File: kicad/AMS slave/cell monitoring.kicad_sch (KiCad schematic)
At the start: 78 parts, among them J1 Conn_02x08_Top_Bottom, Q1 KY2N7002, SW1 SW_Push, U1 BQ76940DBT

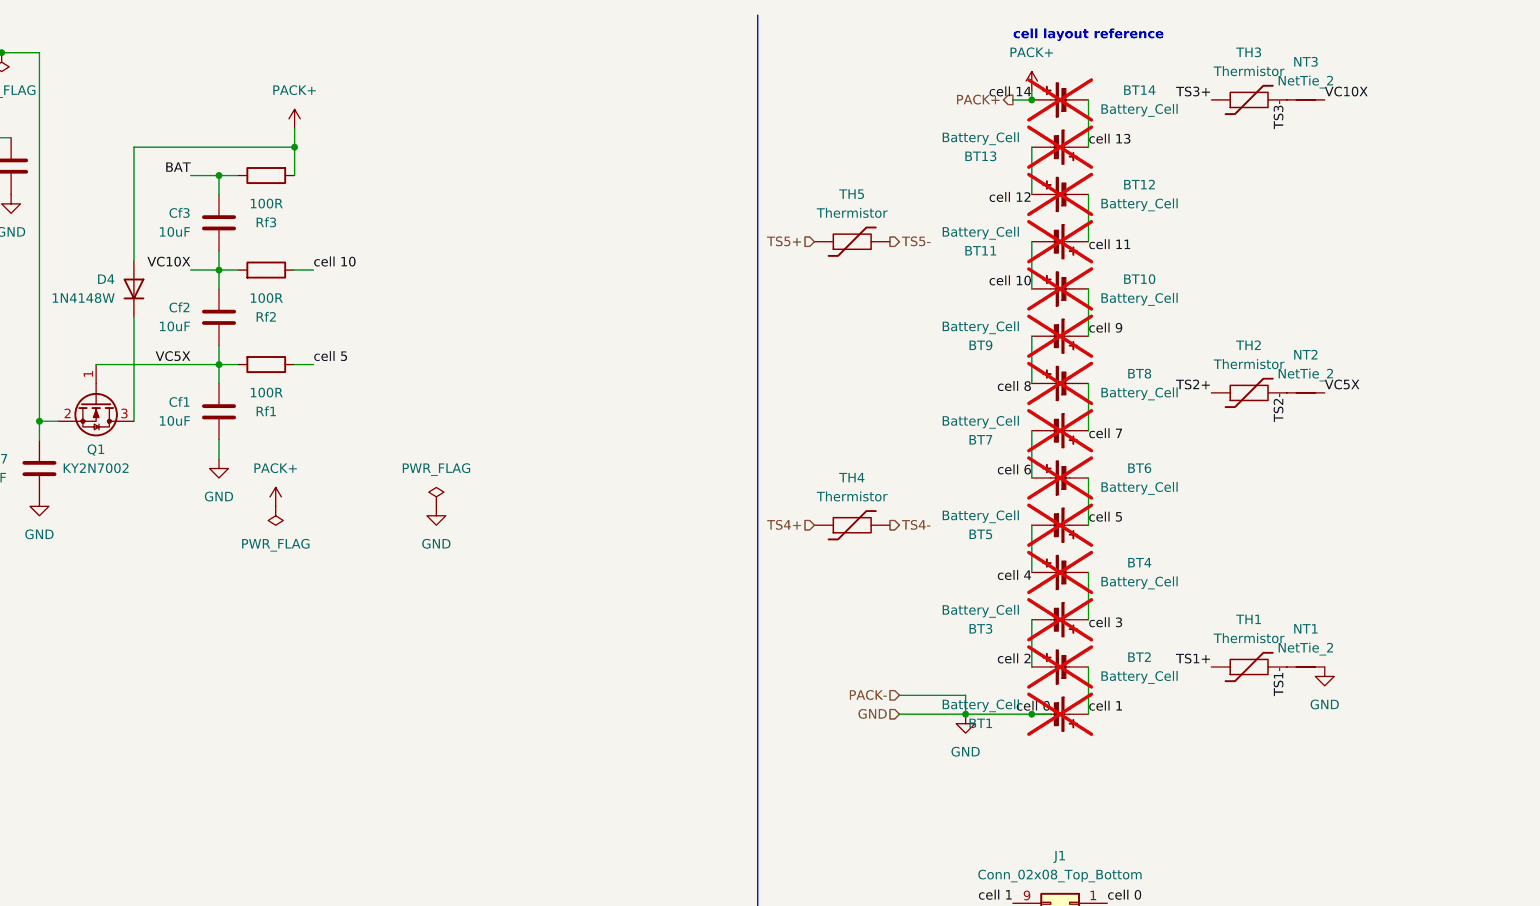
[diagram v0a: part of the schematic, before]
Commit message: AMS slave schem 0.4.3, pcb 0.4.4
schematic: switched out thermistors for 1x02 MP connector symbols, fixed mangled annotations
PCB: switched out thermistor connectors for the correct type
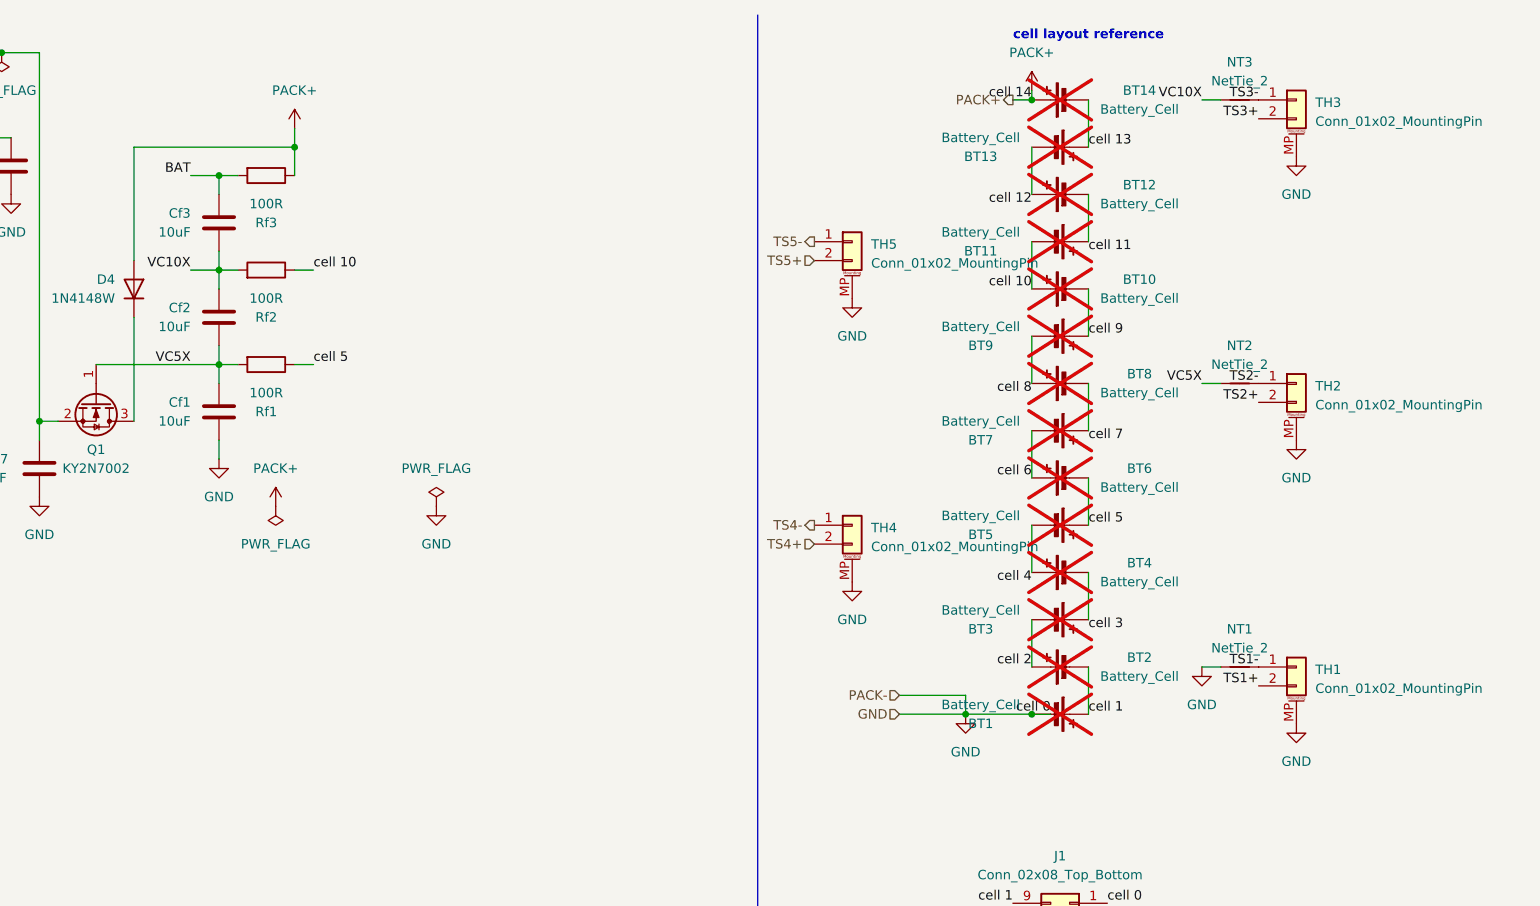
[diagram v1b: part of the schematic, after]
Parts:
- removed TH1, TH2, TH3, TH4, TH5: Thermistor, Connector_JST:JST_PH_S2B-PH-SM4-TB_1x02-1MP_P2.00mm_Horizontal, symbol Device:Thermistor
- added TH1, TH2, TH3, TH4, TH5: Conn_01x02_MountingPin, Connector_Molex:Molex_Micro-Fit_3.0_43650-0210_1x02-1MP_P3.00mm_Horizontal, symbol Connector_Generic_MountingPin:Conn_01x02_MountingPin
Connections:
- net BAT: now also Rf3.2; no longer Rf3.1
- net BQ_RST: now also TH1.2 (Pin_2)
- net GND: now also TH1.MP (MountPin), TH2.MP (MountPin), TH3.MP (MountPin), TH4.MP (MountPin), TH5.MP (MountPin)
- net PACK+: now also Rf3.1; no longer Rf3.2
- net TS1-: now also TH1.1 (Pin_1)
- net TS2+: now also TH2.2 (Pin_2)
- net TS2-: now also TH2.1 (Pin_1)
- net TS3+: now also TH3.2 (Pin_2)
- net TS3-: now also TH3.1 (Pin_1)
- net TS4+: now also TH4.2 (Pin_2)
- net TS4-: now also TH4.1 (Pin_1)
- net TS5+: now also TH5.2 (Pin_2)
- net TS5-: now also TH5.1 (Pin_1)
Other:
- moved on the sheet: NT1, NT3, Rf3

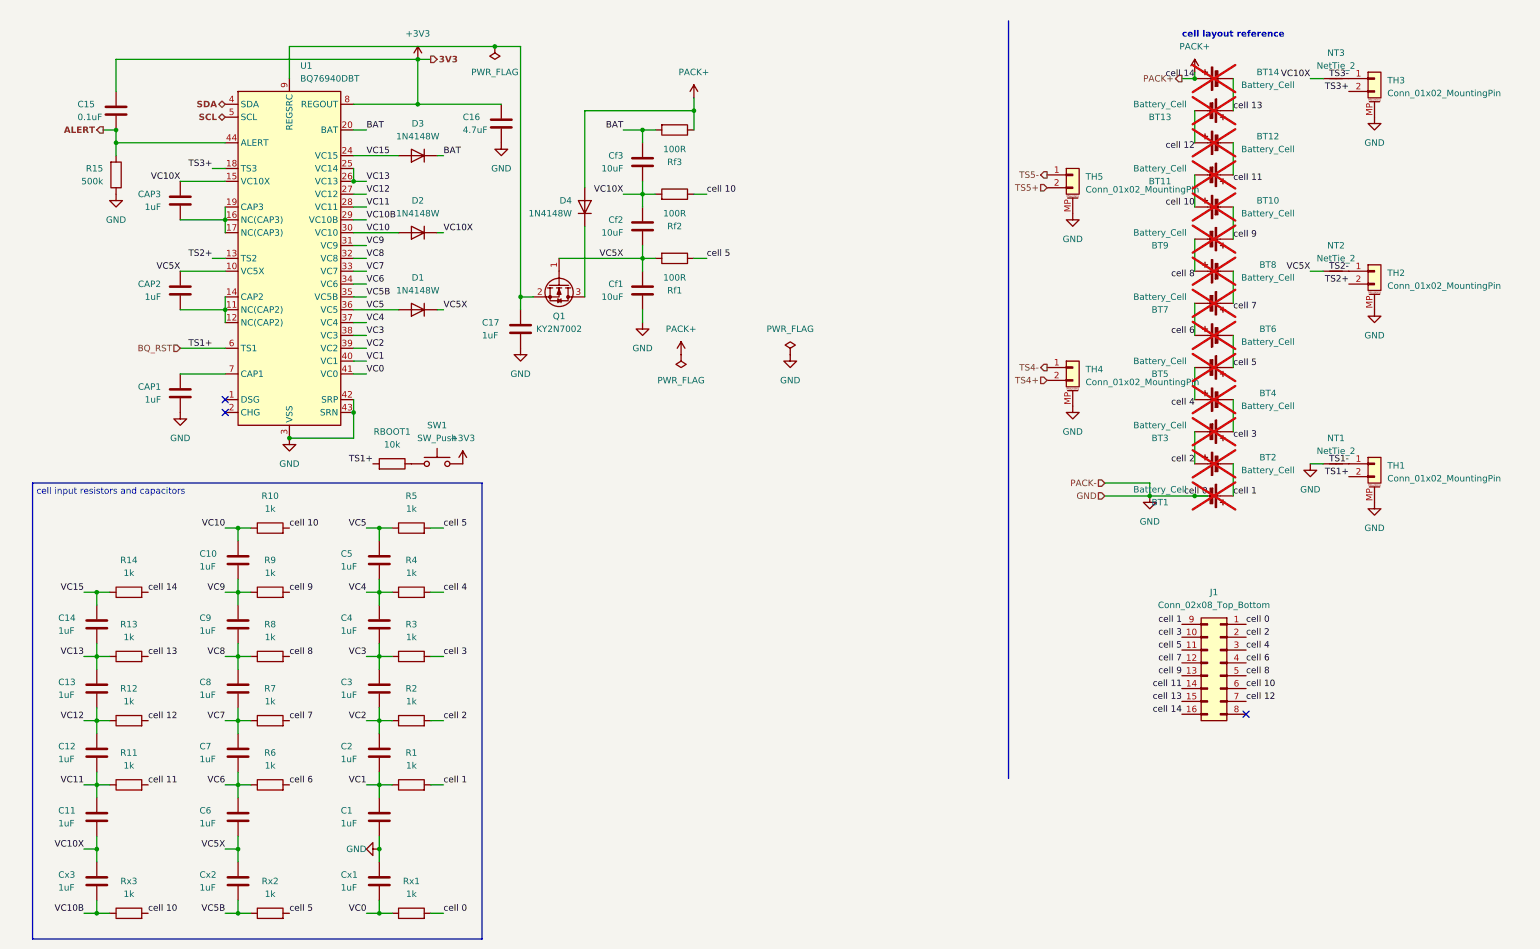
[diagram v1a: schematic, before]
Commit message: AMS slave schem 0.4.4 pcb 0.5.0
schematic cleaned up with labels and removed clipping text
new PCB iteration, with generally shorter traces where applicable, better filter capacitor layout, and pinout labels with silkscreen
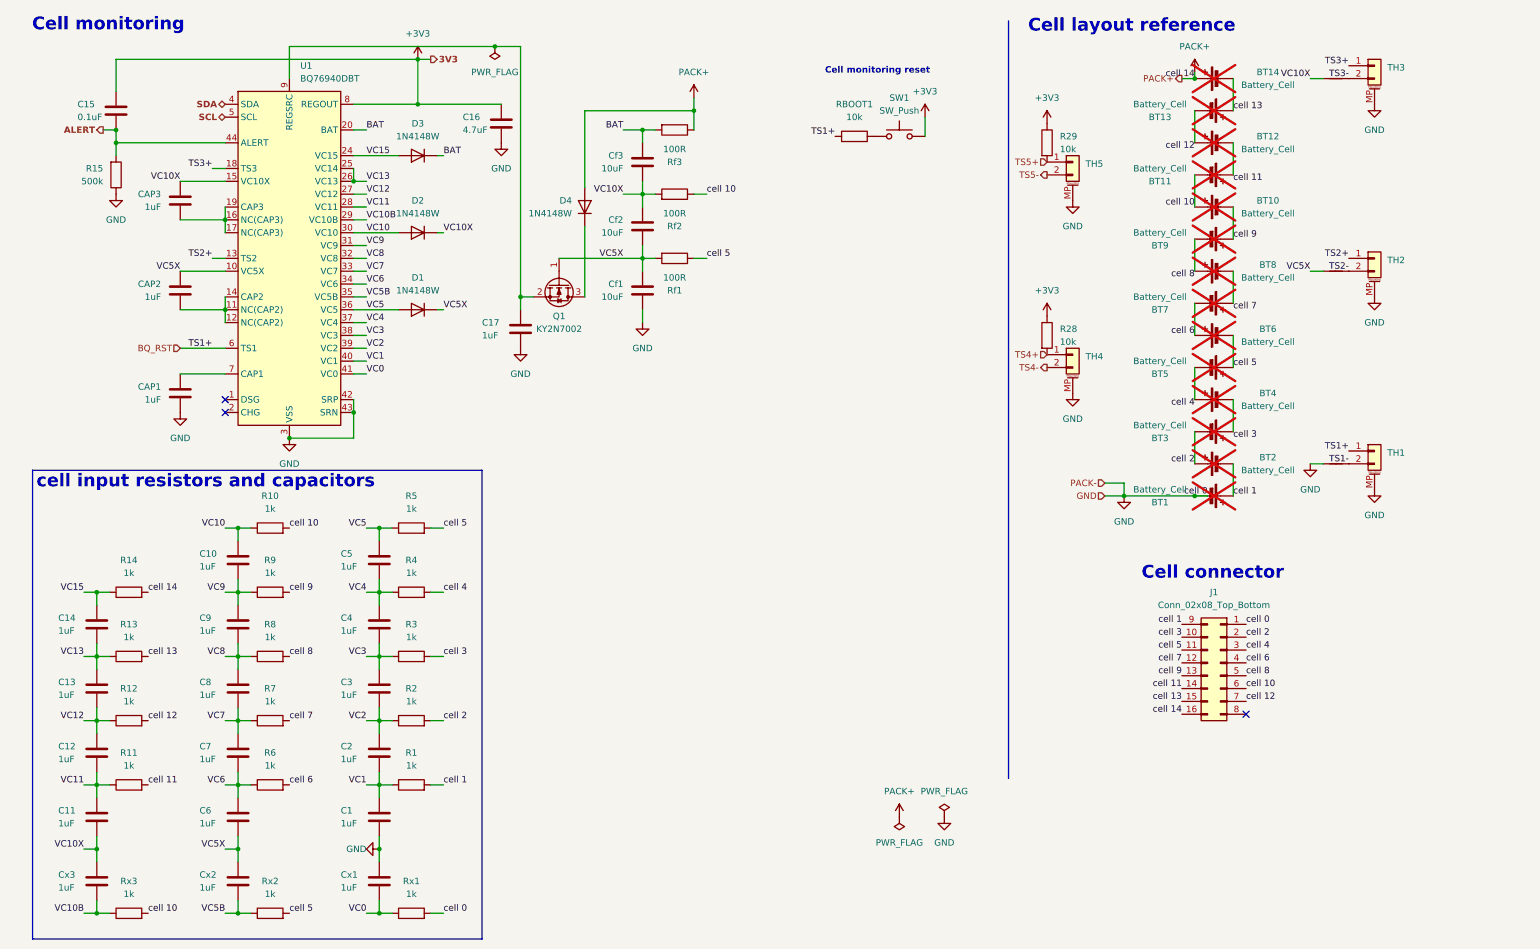
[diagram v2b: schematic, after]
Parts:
- added R28, R29: 10k, RMC_Resistor:R_0805_2012Metric_Pad1.20x1.40mm_HandSolder_L, symbol Device:R
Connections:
- net +3V3: now also SW1.1, R28.1, R29.1; no longer SW1.2
- net BQ_RST: now also TH1.1 (Pin_1); no longer TH1.2 (Pin_2)
- net TS1-: now also TH1.2 (Pin_2); no longer TH1.1 (Pin_1)
- net TS2+: now also TH2.1 (Pin_1); no longer TH2.2 (Pin_2)
- net TS2-: now also TH2.2 (Pin_2); no longer TH2.1 (Pin_1)
- net TS3+: now also TH3.1 (Pin_1); no longer TH3.2 (Pin_2)
- net TS3-: now also TH3.2 (Pin_2); no longer TH3.1 (Pin_1)
- net TS4+: now also TH4.1 (Pin_1), R28.2; no longer TH4.2 (Pin_2)
- net TS4-: now also TH4.2 (Pin_2); no longer TH4.1 (Pin_1)
- net TS5+: now also TH5.1 (Pin_1), R29.2; no longer TH5.2 (Pin_2)
- net TS5-: now also TH5.2 (Pin_2); no longer TH5.1 (Pin_1)
- net at RBOOT1.1: now also SW1.2; no longer SW1.1
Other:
- note added: "Cell connector"
- note added: "Cell layout reference"
- note added: "Cell monitoring"
- note added: "Cell monitoring reset"
- note removed: "cell layout reference"
- title: (none) -> AMS slave cell monitoring
- moved on the sheet: RBOOT1, SW1, TH1, TH2, TH3, TH4, TH5

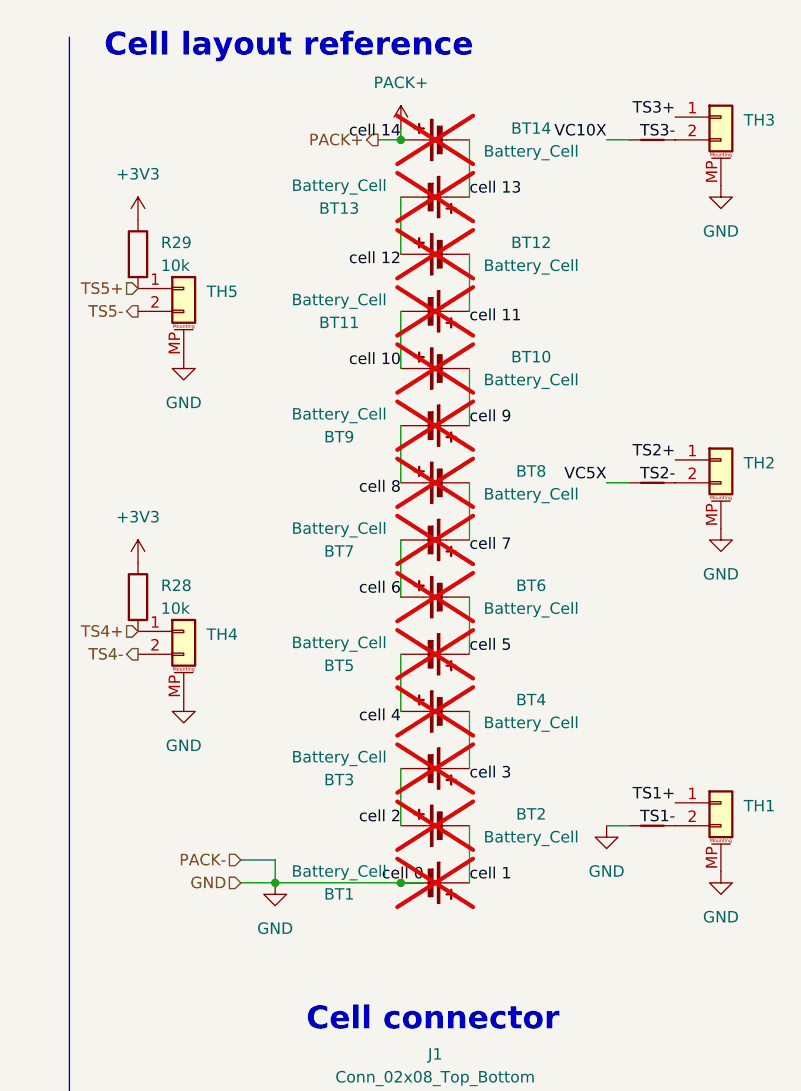
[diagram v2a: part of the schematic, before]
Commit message: AMS slave schem 0.4.5 PCB 0.5.1
PCB: Thermistor connector footprint changed
Adjusted ground traces and other trace position
Schematic: updated thermistor connector symbol
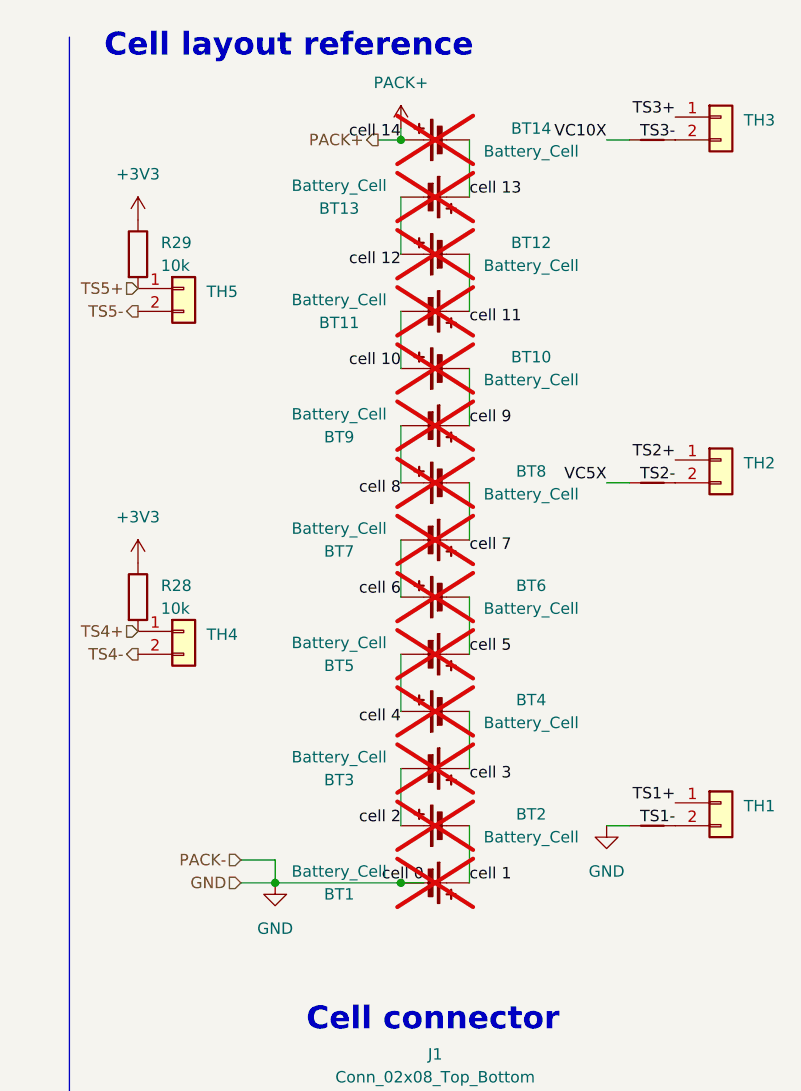
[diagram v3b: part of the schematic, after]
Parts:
- TH1, TH2, TH3, TH4, TH5: footprint Connector_Molex:Molex_Micro-Fit_3.0_43650-0210_1x02-1MP_P3.00mm_Horizontal -> Connector_Molex:Molex_Micro-Fit_3.0_43650-0215_1x02_P3.00mm_Vertical; symbol Connector_Generic_MountingPin:Conn_01x02_MountingPin -> Connector_Generic:Conn_01x02
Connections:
- net GND: no longer TH1.MP (MountPin), TH2.MP (MountPin), TH3.MP (MountPin), TH4.MP (MountPin), TH5.MP (MountPin)
